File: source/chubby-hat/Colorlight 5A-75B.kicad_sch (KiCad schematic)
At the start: 15 parts, among them J10 HUB75, J11 HUB75, J12 HUB75, J13 v7.0, J14 v8.0, J15 HUB75, J16 Conn_01x02, J17 HUB75, J18 HUB75, J19 V7.0, J20 V8.0, J21 HUB75, J22 HUB75

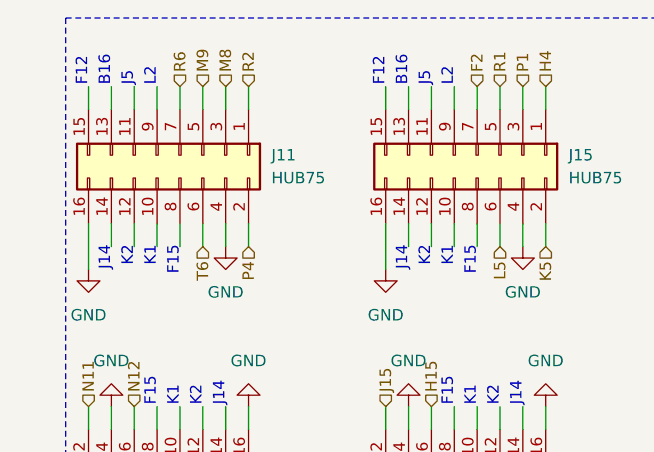
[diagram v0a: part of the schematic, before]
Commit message: switch P4 and R2 on HUB75 J4; closes #5
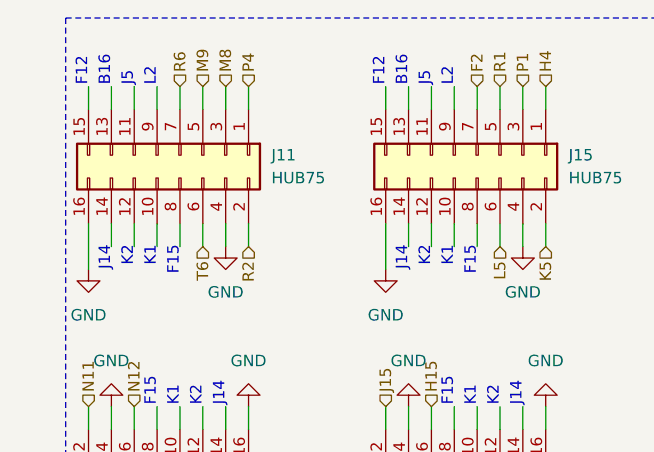
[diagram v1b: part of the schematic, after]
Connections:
- net P4: now also J11.1 (Pin_1); no longer J11.2 (Pin_2)
- net R2: now also J11.2 (Pin_2); no longer J11.1 (Pin_1)
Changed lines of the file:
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@@
     (effects (font (size 1.27 1.27)) (justify left))
   )
-  (hierarchical_label "R2" (shape input) (at 35.56 22.86 90)
-    (effects (font (size 1.27 1.27)) (justify left))
+  (hierarchical_label "R2" (shape input) (at 35.56 40.64 270)
+    (effects (font (size 1.27 1.27)) (justify right))
   )
   (hierarchical_label "G14" (shape input) (at 88.9 76.2 270)
@@
     (effects (font (size 1.27 1.27)) (justify right))
   )
-  (hierarchical_label "P4" (shape input) (at 35.56 40.64 270)
-    (effects (font (size 1.27 1.27)) (justify right))
+  (hierarchical_label "P4" (shape input) (at 35.56 22.86 90)
+    (effects (font (size 1.27 1.27)) (justify left))
   )
   (hierarchical_label "E3" (shape input) (at 93.98 22.86 90)

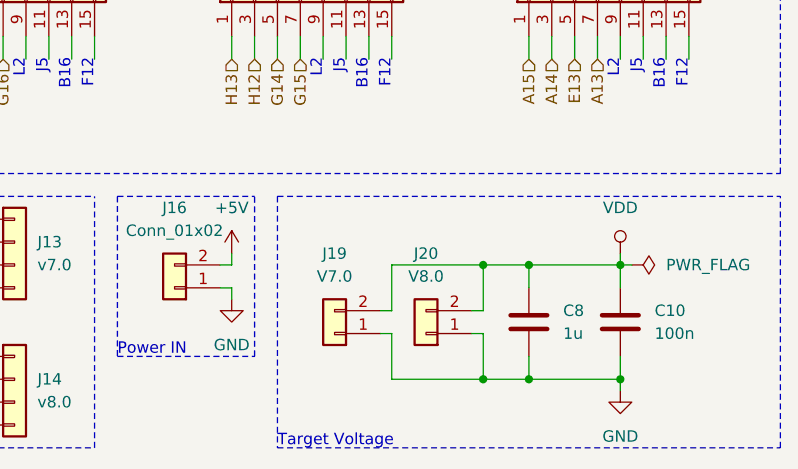
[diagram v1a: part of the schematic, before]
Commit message: add test points and leds - closes #1; add fuse - closes #4; add silk screen art
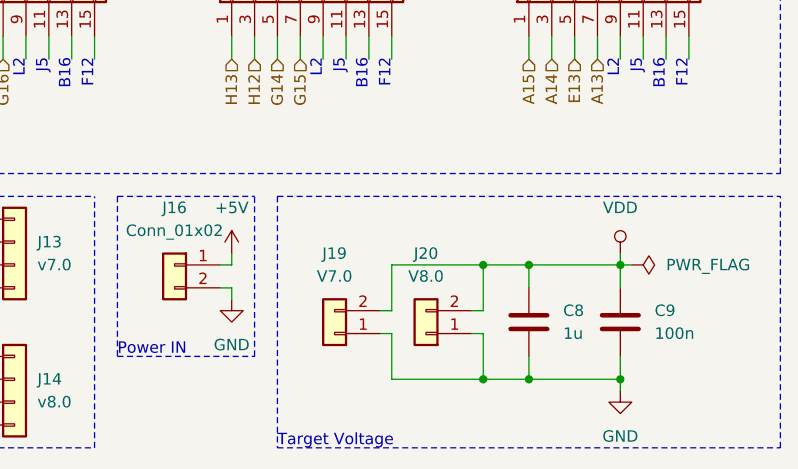
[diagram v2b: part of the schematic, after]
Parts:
- renumbered C10 to C9
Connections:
- net +5V: now also J16.1 (Pin_1); no longer J16.2 (Pin_2)
- net GND: now also J16.2 (Pin_2); no longer J16.1 (Pin_1)
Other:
- moved on the sheet: J16
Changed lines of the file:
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@@
   (symbol (lib_id "power:GND") (at 33.02 40.64 0) (unit 1)
     (in_bom yes) (on_board yes) (fields_autoplaced)
-    (property "Reference" "#PWR062" (id 0) (at 33.02 46.99 0)
+    (property "Reference" "#PWR067" (id 0) (at 33.02 46.99 0)
       (effects (font (size 1.27 1.27)) hide)
     )
@@
   (symbol (lib_id "power:GND") (at 132.08 40.64 0) (unit 1)
     (in_bom yes) (on_board yes) (fields_autoplaced)
-    (property "Reference" "#PWR080" (id 0) (at 132.08 46.99 0)
+    (property "Reference" "#PWR083" (id 0) (at 132.08 46.99 0)
       (effects (font (size 1.27 1.27)) hide)
     )
@@
   (symbol (lib_id "power:GND") (at 83.82 43.18 0) (unit 1)
     (in_bom yes) (on_board yes) (fields_autoplaced)
-    (property "Reference" "#PWR068" (id 0) (at 83.82 49.53 0)
+    (property "Reference" "#PWR073" (id 0) (at 83.82 49.53 0)
       (effects (font (size 1.27 1.27)) hide)
     )
@@
     (pin "9")
   )
-  (symbol (lib_id "Connector_Generic:Conn_01x02") (at 77.47 101.6 180) (unit 1)
+  (symbol (lib_id "Connector_Generic:Conn_01x02") (at 77.47 99.06 0) (mirror y) (unit 1)
     (in_bom yes) (on_board yes) (fields_autoplaced)
     (property "Reference" "J16" (id 0) (at 77.47 92.71 0))
     (property "Value" "Conn_01x02" (id 1) (at 77.47 95.25 0))
-    (property "Footprint" "Connector_Wire:SolderWire-0.5sqmm_1x02_P4.6mm_D0.9mm_OD2.1mm_Relief" (id 2) (at 77.47 101.6 0)
-      (effects (font (size 1.27 1.27)) hide)
-    )
-    (property "Datasheet" "~" (id 3) (at 77.47 101.6 0)
+    (property "Footprint" "Connector_Wire:SolderWire-0.5sqmm_1x02_P4.6mm_D0.9mm_OD2.1mm_Relief" (id 2) (at 77.47 99.06 0)
+      (effects (font (size 1.27 1.27)) hide)
+    )
+    (property "Datasheet" "~" (id 3) (at 77.47 99.06 0)
       (effects (font (size 1.27 1.27)) hide)
     )
@@
   (symbol (lib_id "power:GND") (at 66.04 40.64 0) (unit 1)
     (in_bom yes) (on_board yes) (fields_autoplaced)
-    (property "Reference" "#PWR066" (id 0) (at 66.04 46.99 0)
+    (property "Reference" "#PWR071" (id 0) (at 66.04 46.99 0)
       (effects (font (size 1.27 1.27)) hide)
     )
@@
   (symbol (lib_id "power:GND") (at 127 113.03 0) (mirror y) (unit 1)
     (in_bom yes) (on_board yes) (fields_autoplaced)
-    (property "Reference" "#PWR075" (id 0) (at 127 119.38 0)
+    (property "Reference" "#PWR082" (id 0) (at 127 119.38 0)
       (effects (font (size 1.27 1.27)) hide)
     )
@@
   (symbol (lib_id "power:GND") (at 119.38 58.42 180) (unit 1)
     (in_bom yes) (on_board yes) (fields_autoplaced)
-    (property "Reference" "#PWR079" (id 0) (at 119.38 52.07 0)
+    (property "Reference" "#PWR080" (id 0) (at 119.38 52.07 0)
       (effects (font (size 1.27 1.27)) hide)
     )
@@
   (symbol (lib_id "power:GND") (at 53.34 58.42 180) (unit 1)
     (in_bom yes) (on_board yes) (fields_autoplaced)
-    (property "Reference" "#PWR065" (id 0) (at 53.34 52.07 0)
+    (property "Reference" "#PWR070" (id 0) (at 53.34 52.07 0)
       (effects (font (size 1.27 1.27)) hide)
     )
@@
   (symbol (lib_id "power:GND") (at 83.82 102.87 0) (mirror y) (unit 1)
     (in_bom yes) (on_board yes) (fields_autoplaced)
-    (property "Reference" "#PWR070" (id 0) (at 83.82 109.22 0)
+    (property "Reference" "#PWR075" (id 0) (at 83.82 109.22 0)
       (effects (font (size 1.27 1.27)) hide)
     )
@@
   (symbol (lib_id "power:VDD") (at 127 97.79 0) (mirror y) (unit 1)
     (in_bom yes) (on_board yes) (fields_autoplaced)
-    (property "Reference" "#PWR074" (id 0) (at 127 101.6 0)
+    (property "Reference" "#PWR081" (id 0) (at 127 101.6 0)
       (effects (font (size 1.27 1.27)) hide)
     )
@@
   (symbol (lib_id "power:GND") (at 68.58 58.42 180) (unit 1)
     (in_bom yes) (on_board yes) (fields_autoplaced)
-    (property "Reference" "#PWR067" (id 0) (at 68.58 52.07 0)
+    (property "Reference" "#PWR072" (id 0) (at 68.58 52.07 0)
       (effects (font (size 1.27 1.27)) hide)
     )
@@
   (symbol (lib_id "power:GND") (at 35.56 58.42 180) (unit 1)
     (in_bom yes) (on_board yes) (fields_autoplaced)
-    (property "Reference" "#PWR063" (id 0) (at 35.56 52.07 0)
+    (property "Reference" "#PWR068" (id 0) (at 35.56 52.07 0)
       (effects (font (size 1.27 1.27)) hide)
     )
@@
   (symbol (lib_id "Device:C") (at 127 105.41 0) (mirror x) (unit 1)
     (in_bom yes) (on_board yes) (fields_autoplaced)
-    (property "Reference" "C10" (id 0) (at 130.81 104.1399 0)
+    (property "Reference" "C9" (id 0) (at 130.81 104.1399 0)
       (effects (font (size 1.27 1.27)) (justify left))
     )
@@
   (symbol (lib_id "power:GND") (at 17.78 43.18 0) (unit 1)
     (in_bom yes) (on_board yes) (fields_autoplaced)
-    (property "Reference" "#PWR060" (id 0) (at 17.78 49.53 0)
+    (property "Reference" "#PWR065" (id 0) (at 17.78 49.53 0)
       (effects (font (size 1.27 1.27)) hide)
     )
@@
   (symbol (lib_id "power:GND") (at 134.62 55.88 180) (unit 1)
     (in_bom yes) (on_board yes) (fields_autoplaced)
-    (property "Reference" "#PWR081" (id 0) (at 134.62 49.53 0)
+    (property "Reference" "#PWR084" (id 0) (at 134.62 49.53 0)
       (effects (font (size 1.27 1.27)) hide)
     )
@@
   (symbol (lib_id "power:GND") (at 99.06 40.64 0) (unit 1)
     (in_bom yes) (on_board yes) (fields_autoplaced)
-    (property "Reference" "#PWR072" (id 0) (at 99.06 46.99 0)
+    (property "Reference" "#PWR077" (id 0) (at 99.06 46.99 0)
       (effects (font (size 1.27 1.27)) hide)
     )
@@
   (symbol (lib_id "power:+5V") (at 83.82 97.79 0) (mirror y) (unit 1)
     (in_bom yes) (on_board yes) (fields_autoplaced)
-    (property "Reference" "#PWR069" (id 0) (at 83.82 101.6 0)
+    (property "Reference" "#PWR074" (id 0) (at 83.82 101.6 0)
       (effects (font (size 1.27 1.27)) hide)
     )
@@
   (symbol (lib_id "power:GND") (at 20.32 58.42 180) (unit 1)
     (in_bom yes) (on_board yes) (fields_autoplaced)
-    (property "Reference" "#PWR061" (id 0) (at 20.32 52.07 0)
+    (property "Reference" "#PWR066" (id 0) (at 20.32 52.07 0)
       (effects (font (size 1.27 1.27)) hide)
     )
@@
   (symbol (lib_id "power:GND") (at 86.36 58.42 180) (unit 1)
     (in_bom yes) (on_board yes) (fields_autoplaced)
-    (property "Reference" "#PWR071" (id 0) (at 86.36 52.07 0)
+    (property "Reference" "#PWR076" (id 0) (at 86.36 52.07 0)
       (effects (font (size 1.27 1.27)) hide)
     )
@@
   (symbol (lib_id "power:GND") (at 116.84 40.64 0) (unit 1)
     (in_bom yes) (on_board yes) (fields_autoplaced)
-    (property "Reference" "#PWR078" (id 0) (at 116.84 46.99 0)
+    (property "Reference" "#PWR079" (id 0) (at 116.84 46.99 0)
       (effects (font (size 1.27 1.27)) hide)
     )
@@
   (symbol (lib_id "power:GND") (at 50.8 43.18 0) (unit 1)
     (in_bom yes) (on_board yes) (fields_autoplaced)
-    (property "Reference" "#PWR064" (id 0) (at 50.8 49.53 0)
+    (property "Reference" "#PWR069" (id 0) (at 50.8 49.53 0)
       (effects (font (size 1.27 1.27)) hide)
     )
@@
   (symbol (lib_id "power:GND") (at 101.6 58.42 180) (unit 1)
     (in_bom yes) (on_board yes) (fields_autoplaced)
-    (property "Reference" "#PWR073" (id 0) (at 101.6 52.07 0)
-      (effects (font (size 1.27 1.27)) hide)
-    )
+    (property "Reference" "#PWR078" (id 0) (at 101.6 52.07 0)
+      (effects (font (size 1.27 1.27)) hide)
+    )

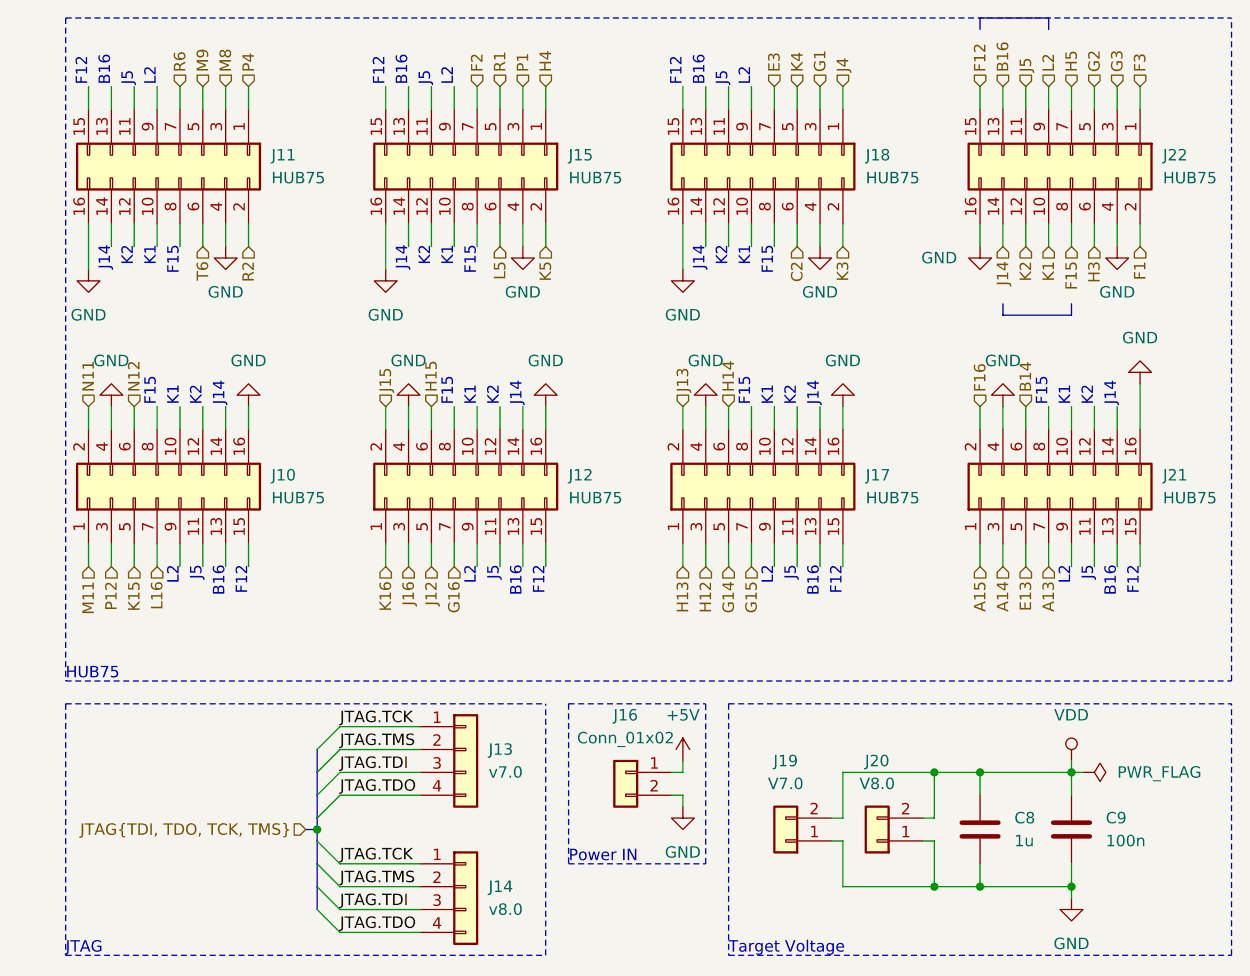
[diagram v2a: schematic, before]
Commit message: add zero volt diodes to USB and modules; add status LEDs; add RP2040 SWD - closes #9
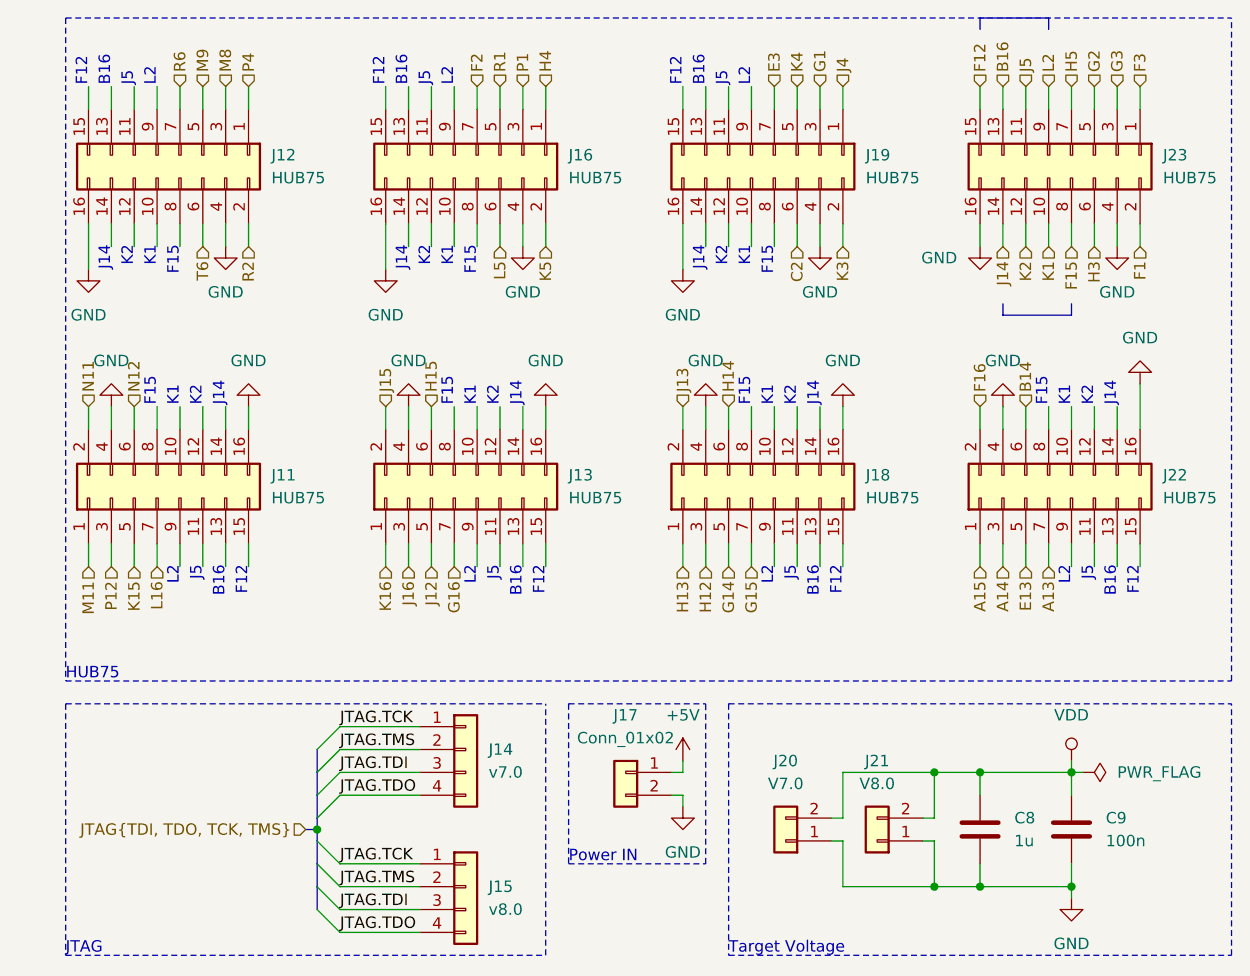
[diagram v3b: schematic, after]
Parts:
- renumbered J10 to J11, J11 to J12, J12 to J13, J13 to J14, J14 to J15, J15 to J16, J16 to J17, J17 to J18, J18 to J19, J19 to J20, J20 to J21, J21 to J22, J22 to J23
